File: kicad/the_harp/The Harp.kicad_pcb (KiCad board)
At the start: 4 copper layers, 56 x 94.5 mm, 181 parts, among them IC501 AK4621EF, J401 PJ-063AH, J402 NMJ6HCD2, J403 NMJ6HCD2, J404 NMJ6HCD2, J405 Bypass FSW, J406 NMJ6HCD2, J407 Hold FSW, J408 OLED 0.91 128x32, K401 G6K-2F-Y, Q401 2N7002, Q402 2N7002, Q403 2N7002, SW101 100-DP6, SW102 100-DP6, SW103 100-DP6, U201 STM32H750VBT6, U202 W25Q128JVSIQ, U301 TPS54202DDC, U302 NCP718ASN500T1G, U401 MCP6001T-I/OT, U501 OPA2348AIDR, U601 THS4522IPW, U701 OPA2365AIDR, U702 OPA1688IDR, Y201 25MHz 9pF

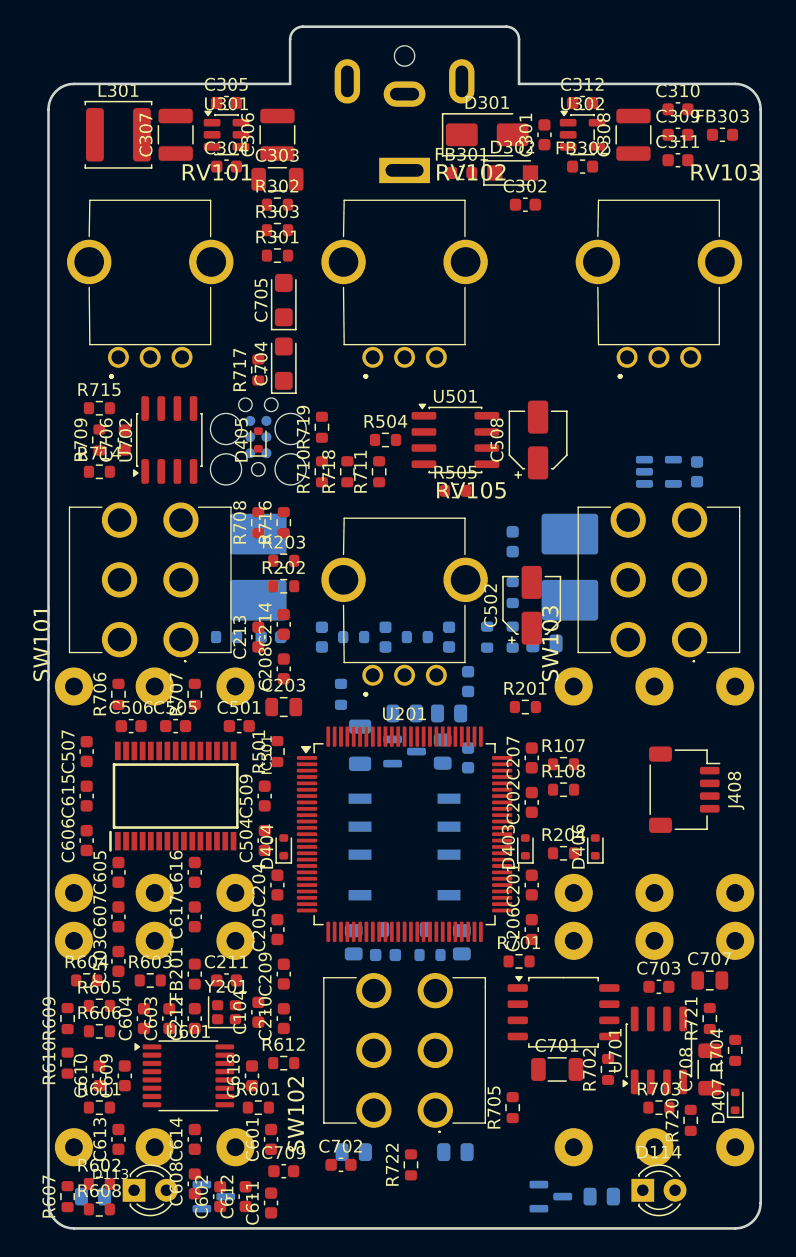
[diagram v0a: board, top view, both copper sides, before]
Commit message: Route the board by script (in progress): GND and rail fanout, In2 rails, power, core digital, audio
Freerouting 2.4.1 driven per net class from scripts/pcb_routing/: every SMD
GND pad its own via to In1, rails on In2 only, analog and digital kept in
their own regions, signals never on In2. Core digital and audio routed;
12 connections still open, drive/ctrl/repair phases to follow. Net classes
written into the project.

Co-Authored-By: Claude Opus 5.5 <noreply@anthropic.com>
Claude-Session: https://claude.ai/code/session_016hDejPHPgG8auBLMyByYZK
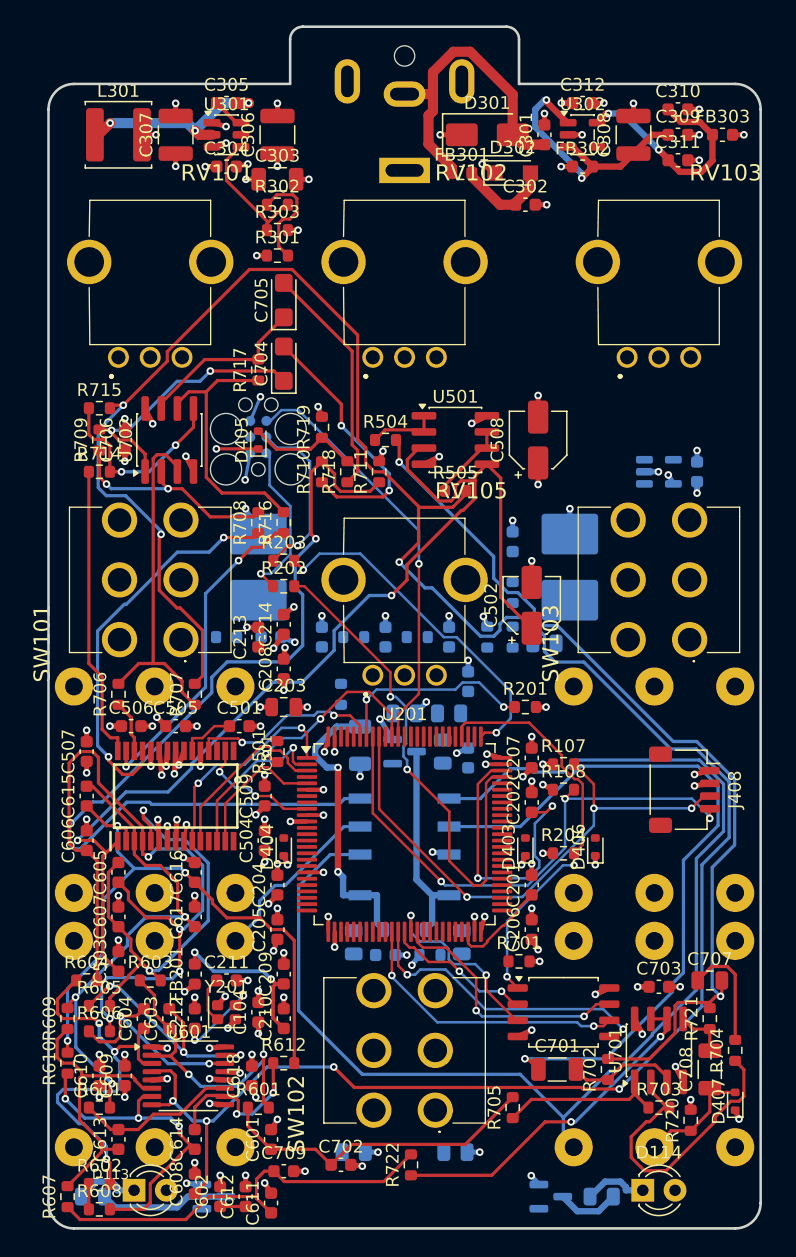
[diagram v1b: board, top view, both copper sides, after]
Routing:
- net +3V3: track 0.00 -> 320.0 mm, vias 0 -> 34
- net +9V: track 0.00 -> 239.0 mm, vias 0 -> 6
- net +5V: track 0.00 -> 206.4 mm, vias 0 -> 19
- net VCOM_B: track 0.00 -> 192.7 mm, vias 0 -> 7
- net GND: track 0.00 -> 113.4 mm, vias 0 -> 106
- net /Jacks and Bypass/IN: track 0.00 -> 98.2 mm
- net /Codec/VCOM: track 0.00 -> 85.5 mm, vias 0 -> 2
- net VCOM_A: track 0.00 -> 75.9 mm, vias 0 -> 2
- net EFFECT_OUT_L: track 0.00 -> 73.4 mm, vias 0 -> 1
- net ADC_L_P: track 0.00 -> 62.6 mm, vias 0 -> 4
- net EFFECT_IN: track 0.00 -> 56.6 mm, vias 0 -> 1
- net ADC_R_P: track 0.00 -> 50.1 mm, vias 0 -> 3
- net OLED_SCL: track 0.00 -> 42.8 mm, vias 0 -> 3
- net OLED_SDA: track 0.00 -> 42.4 mm, vias 0 -> 3
- net /MCU/SWDIO: track 0.00 -> 40.5 mm, vias 0 -> 2
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
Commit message: Routing: drive, control and rip-up repair phases; 32 connections left for KiCad
Core digital before audio, the long LED/relay drive lines after it; jack and
pot pins reach only 1.5 mm into the analog/digital regions; the repair pass
unlocks the signal tracks so the router can move them. Geometric dedupe of
the session's repeated copper. 1546 tracks, 302 vias, scripted check clean;
the open connections are listed in docs/pcb-plan.md (Routing).

Co-Authored-By: Claude Opus 5.5 <noreply@anthropic.com>
Claude-Session: https://claude.ai/code/session_016hDejPHPgG8auBLMyByYZK
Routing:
- net EXP: track 0.00 -> 62.7 mm, vias 0 -> 3
- net /Jacks and Bypass/EXP_BUF_IN: track 0.00 -> 47.6 mm, vias 0 -> 2
- net FSW_HOLD_IN: track 0.00 -> 36.4 mm, vias 0 -> 1
- net /MCU/HSE_IN: track 3.71 -> 39.7 mm, vias 0 -> 2
- net POT5: track 0.00 -> 34.0 mm, vias 0 -> 3
- net /Jacks and Bypass/LED_EFF_G: track 0.00 -> 32.8 mm, vias 0 -> 2
- net /Jacks and Bypass/EXP_BUF_OUT: track 0.00 -> 30.4 mm, vias 0 -> 2
- net /Controls and LEDs/POT1_W: track 0.00 -> 29.9 mm, vias 0 -> 2
- net TOG2_A: track 0.00 -> 27.9 mm, vias 0 -> 2
- net /Jacks and Bypass/EXP_TIP: track 0.00 -> 27.4 mm, vias 0 -> 1
- net /Jacks and Bypass/RELAY_G: track 0.00 -> 26.9 mm, vias 0 -> 4
- net /Jacks and Bypass/FSW_HOLD: track 0.00 -> 19.5 mm, vias 0 -> 2
- net /Controls and LEDs/POT5_W: track 0.00 -> 12.8 mm, vias 0 -> 1
- net POT2: track 0.00 -> 10.8 mm, vias 0 -> 2
- net EFFECT_IN: track 56.6 -> 66.3 mm
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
